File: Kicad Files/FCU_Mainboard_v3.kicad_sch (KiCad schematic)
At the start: 12 parts, among them U5 ATMega2560

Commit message: New routing with thicker 5V and 3V lines, better arrangement. Removed the useless RX and TX leds, they weren't really working as intended.
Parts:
- XT16MHz1: footprint Crystal:Crystal_SMD_EuroQuartz_MJ-4Pin_5.0x3.2mm_HandSoldering -> Crystal:Crystal_SMD_EuroQuartz_MQ-4Pin_7.0x5.0mm_HandSoldering
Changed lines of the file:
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@@
 			)
 		)
-		(property "Footprint" "Crystal:Crystal_SMD_EuroQuartz_MJ-4Pin_5.0x3.2mm_HandSoldering"
+		(property "Footprint" "Crystal:Crystal_SMD_EuroQuartz_MQ-4Pin_7.0x5.0mm_HandSoldering"
 			(at 134.62 166.37 0)
 			(effects

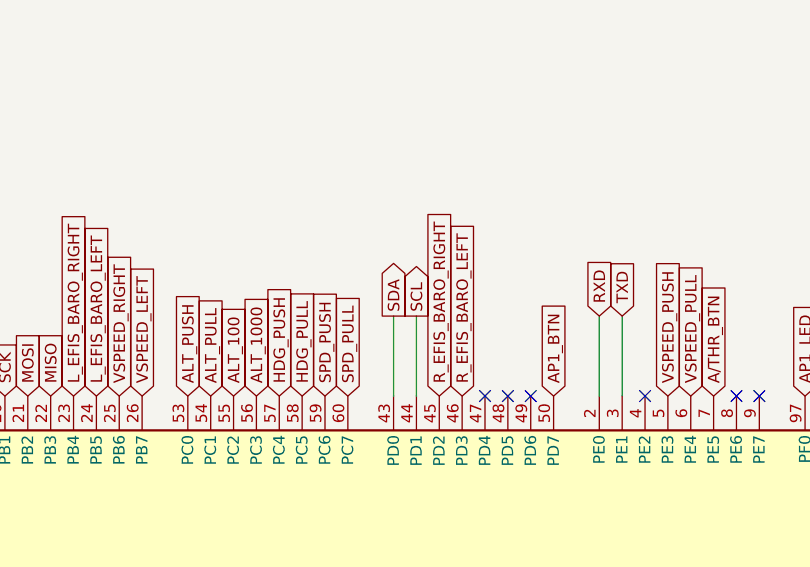
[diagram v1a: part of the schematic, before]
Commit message: Complete rework of panels to be printed facedown. Important: change the order of the colors as Grey, White, Black, Transparent if using a Bambulab P1S/X1C ALso corrected some issue with the PCB (optional, you can print the FCU without using my pcb)
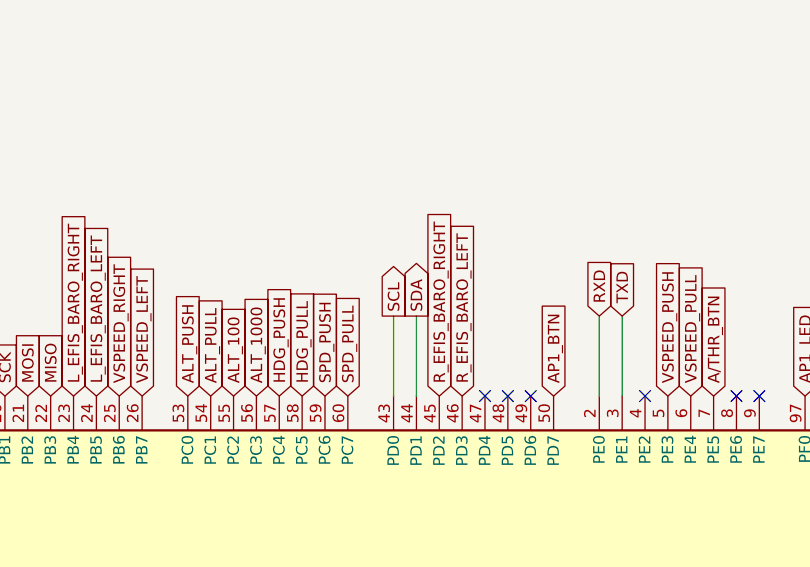
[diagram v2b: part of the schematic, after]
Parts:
- U5: footprint SFLibrary:TQFP100-0.5-14X14MM -> PCM_SFLibrary:TQFP100-0.5-14X14MM
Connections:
- net SCL: now also U5.43 (PD0); no longer U5.44 (PD1)
- net SDA: now also U5.44 (PD1); no longer U5.43 (PD0)
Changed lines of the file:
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@@
 (kicad_sch
-	(version 20231120)
+	(version 20250114)
 	(generator "eeschema")
-	(generator_version "8.0")
+	(generator_version "9.0")
 	(paper "A4")
 	(title_block
@@
 		)
 	)
+	(global_label "SCL"
+		(shape output)
+		(at 166.37 78.74 90)
+		(fields_autoplaced yes)
+		(effects
+			(font
+				(size 1.27 1.27)
+			)
+			(justify left)
+		)
+		(property "Intersheetrefs" "${INTERSHEET_REFS}"
+			(at 166.37 72.2472 90)
+			(effects
+				(font
+					(size 1.27 1.27)
+				)
+				(justify left)
+				(hide yes)
+			)
+		)
+	)
 	(global_label "R_EFIS_LS_LED"
 		(shape input)
@@
 		)
 	)
-	(global_label "SCL"
-		(shape output)
-		(at 168.91 78.74 90)
-		(fields_autoplaced yes)
-		(effects
-			(font
-				(size 1.27 1.27)
-			)
-			(justify left)
-		)
-		(property "Intersheetrefs" "${INTERSHEET_REFS}"
-			(at 168.91 72.2472 90)
-			(effects
-				(font
-					(size 1.27 1.27)
-				)
-				(justify left)
-				(hide yes)
-			)
-		)
-	)
 	(global_label "GND"
 		(shape input)
@@
 		)
 	)
+	(global_label "SDA"
+		(shape output)
+		(at 168.91 78.74 90)
+		(fields_autoplaced yes)
+		(effects
+			(font
+				(size 1.27 1.27)
+			)
+			(justify left)
+		)
+		(property "Intersheetrefs" "${INTERSHEET_REFS}"
+			(at 168.91 72.1867 90)
+			(effects
+				(font
+					(size 1.27 1.27)
+				)
+				(justify left)
+				(hide yes)
+			)
+		)
+	)
 	(global_label "A{slash}THR_LED"
 		(shape input)
@@
 		)
 	)
-	(global_label "SDA"
-		(shape output)
-		(at 166.37 78.74 90)
-		(fields_autoplaced yes)
-		(effects
-			(font
-				(size 1.27 1.27)
-			)
-			(justify left)
-		)
-		(property "Intersheetrefs" "${INTERSHEET_REFS}"
-			(at 166.37 72.1867 90)
-			(effects
-				(font
-					(size 1.27 1.27)
-				)
-				(justify left)
-				(hide yes)
-			)
-		)
-	)
 	(global_label "L_EFIS_BARO_LEFT"
 		(shape input)
@@
 			)
 		)
-		(property "Footprint" "SFLibrary:TQFP100-0.5-14X14MM"
+		(property "Footprint" "PCM_SFLibrary:TQFP100-0.5-14X14MM"
 			(at 163.83 107.95 0)
 			(effects
@@
 		(at 612.14 227.33)
 		(size 275.59 204.47)
+		(exclude_from_sim no)
+		(in_bom yes)
+		(on_board yes)
+		(dnp no)
 		(fields_autoplaced yes)
 		(stroke
@@
 		(at 0 227.33)
 		(size 298.45 205.74)
+		(exclude_from_sim no)
+		(in_bom yes)
+		(on_board yes)
+		(dnp no)
 		(fields_autoplaced yes)
 		(stroke
@@
 		(at 331.47 0)
 		(size 265.43 204.47)
+		(exclude_from_sim no)
+		(in_bom yes)
+		(on_board yes)
+		(dnp no)
 		(fields_autoplaced yes)
 		(stroke
@@
 		(at 331.47 227.33)
 		(size 266.7 205.74)
+		(exclude_from_sim no)
+		(in_bom yes)
+		(on_board yes)
+		(dnp no)
 		(fields_autoplaced yes)
 		(stroke
@@
 		(at 609.6 0)
 		(size 278.13 215.9)
+		(exclude_from_sim no)
+		(in_bom yes)
+		(on_board yes)
+		(dnp no)
 		(fields_autoplaced yes)
 		(stroke
@@
 		)
 	)
+	(embedded_fonts no)
 )
